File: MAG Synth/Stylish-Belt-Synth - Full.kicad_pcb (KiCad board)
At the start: 2 copper layers, 177.8 x 101.7 mm, 67 parts, among them J0 USB_B, J1 Audio-Jack-3_2Switches, J26 WRITE PATCH, J27 PARAM SELECT, J28 PATCH SELECT, J29 MODE, J30 STYLUS, SW1 Power, U1 stm32f103c8t6-module-china, U2 XPT8871

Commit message: V3 board V2.4 case
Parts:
- removed BT1: 4 x 1.5V, Pin_Headers:Pin_Header_Straight_1x02_Pitch2.54mm
- removed BT2: Conn_01x02, Pin_Headers:Pin_Header_Straight_1x02_Pitch2.54mm
- removed JA1: Conn_01x06, Pin_Headers:Pin_Header_Straight_1x06_Pitch2.54mm
- removed JL1: ~, Pin_Headers:Pin_Header_Straight_1x04_Pitch2.54mm
- removed the REF** at (215.1, 104.8)
- removed the REF** at (82.9, 104.6)
- added ?: 1pin, Connect:1pin, F.Cu at (79.2, 66.4)
- added ?: 1pin, Connect:1pin, F.Cu at (222.1, 70.2)
- added BT12: ~, SoftEggKiCAD:AA_Battery_Dual_Terminal, B.Cu at (95.2, 134.2)
- added BT34: ~, SoftEggKiCAD:AA_Battery_Dual_Terminal, B.Cu at (187.3, 134.0)
- added BTN1: -, SoftEggKiCAD:AA_Battery_-_Terminal, B.Cu at (109.2, 78.1)
- added BTN3: -, SoftEggKiCAD:AA_Battery_-_Terminal, B.Cu at (201.3, 78.1)
- added BTP2: +, SoftEggKiCAD:AA_Battery_+_Terminal, B.Cu at (95.2, 78.1)
- added BTP4: +, SoftEggKiCAD:AA_Battery_+_Terminal, B.Cu at (187.3, 78.1)
- added C2: 1000μF, Capacitors_ThroughHole:CP_Radial_D10.0mm_P5.00mm, B.Cu at (194.2, 66.3)
- added C3: 470μF, Capacitors_ThroughHole:CP_Radial_D10.0mm_P5.00mm, B.Cu at (183.4, 66.3)
- added RA1: 100Ω, SoftEggKiCAD:R_Axial_DIN0204_L3.6mm_D1.6mm_P7.62mm_Horizontal+SMD804, F.Cu at (108.0, 64.1)
- added REF**: 1pin, Connectors:1pin, F.Cu at (215.9, 82.5)
- added REF**: 1pin, Connectors:1pin, F.Cu at (215.9, 91.4)
- added RV1: Volume, SoftEggKiCAD:Wheel_Pot_W_Switch_RV12_B103_FUSTAR, B.Cu at (94.2, 59.4)
- CA1: footprint Capacitors_ThroughHole:CP_Radial_Tantal_D4.5mm_P2.50mm -> SoftEggKiCAD:C_Disc_D5.0mm_W2.5mm_P5.00mm+SMD
- CA3: footprint SoftEggKiCAD:C_Disc_D5.0mm_W2.5mm_P5.00mm+SMD -> Capacitors_ThroughHole:CP_Radial_Tantal_D4.5mm_P2.50mm
- CA4: moved to F.Cu
- J1: value Audio-Jack-3_2Switches -> Headphone
- LS1: value SPEAKER -> Speaker
- R1: value 10kΩ -> 8Ω
- R2: value 1k -> 47Ω
- R3: value 100Ω -> 120Ω; moved to F.Cu
- SW1: value Power -> OVERDRIVE; footprint SoftEggKiCAD:MSS22D18+THT -> Pin_Headers:Pin_Header_Straight_1x03_Pitch2.54mm; moved to B.Cu
- moved G*** 96.7 mm to (196.8, 86.7)
- moved CA4 83.0 mm to (104.8, 58.3), turned to 270 degrees
- moved R2 79.6 mm to (100.6, 66.5)
- moved D3 78.3 mm to (87.6, 72.4), turned to 180 degrees
- moved C1 76.5 mm to (114.9, 67.0), turned to 270 degrees
- moved R1 76.3 mm to (111.8, 66.8), turned to 270 degrees
- moved SW1 70.9 mm to (108.6, 70.5), turned to 90 degrees
- moved R3 67.6 mm to (125.2, 108.1)
- moved CA1 39.9 mm to (174.0, 56.8), turned to 270 degrees
- moved U2 36.5 mm to (189.2, 61.0), turned to 90 degrees
- moved CA2 35.0 mm to (177.8, 56.5), turned to 270 degrees
- moved CA3 34.0 mm to (181.9, 59.7)
- moved D4 31.8 mm to (87.6, 70.0), turned to 0 degrees
- moved D1 16.1 mm to (102.4, 83.1), turned to 180 degrees
- moved CL0 6.46 mm to (148.5, 60.2), turned to 45 degrees
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- renumbered REF** to ?
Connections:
- C1 pad 1: /PWM_OUT -> Net-(C1-Pad1)
- C1 pad 2: Net-(C1-Pad2) -> GND
- CL0 pad 1: /+5V -> /VIN
- CL1 pad 1: /+5V -> /VIN
- CL10 pad 1: /+5V -> /VIN
- CL11 pad 1: /+5V -> /VIN
- CL12 pad 1: /+5V -> /VIN
- CL13 pad 1: /+5V -> /VIN
- CL14 pad 1: /+5V -> /VIN
- CL15 pad 1: /+5V -> /VIN
- CL2 pad 1: /+5V -> /VIN
- CL3 pad 1: /+5V -> /VIN
- CL4 pad 1: /+5V -> /VIN
- CL5 pad 1: /+5V -> /VIN
- CL6 pad 1: /+5V -> /VIN
- CL7 pad 1: /+5V -> /VIN
- CL8 pad 1: /+5V -> /VIN
- CL9 pad 1: /+5V -> /VIN
- D3 pad 1: /+5V -> /VUSB
- D3 pad 2: Net-(D3-Pad2) -> Net-(BTP4-Pad1)
- D4 pad 1: /+5V -> /VUSB
- J1 pad 1: /XH-M125-amp-board/OUT+ -> Net-(J1-Pad1)
- J1 pad 2: /XH-M125-amp-board/OUT+ -> Net-(J1-Pad1)
- J1 pad 3: /XH-M125-amp-board/OUT- -> Net-(J1-Pad3)
- LS1 pad 2: /XH-M125-amp-board/OUT- -> Net-(J1-Pad3)
- R1 pad 1: Net-(C1-Pad2) -> Net-(C1-Pad1)
- R2 pad 1: GND -> Net-(R2-Pad1)
- R2 pad 2: Net-(C1-Pad2) -> Net-(C1-Pad1)
- R3 pad 1: Net-(R3-Pad1) -> /VIN
- R3 pad 2: Net-(CA4-Pad1) -> /+3.3V
- RGB0 pad 1: /+5V -> /VIN
- RGB1 pad 1: /+5V -> /VIN
- RGB10 pad 1: /+5V -> /VIN
- RGB11 pad 1: /+5V -> /VIN
- RGB12 pad 1: /+5V -> /VIN
- RGB13 pad 1: /+5V -> /VIN
- RGB14 pad 1: /+5V -> /VIN
- RGB15 pad 1: /+5V -> /VIN
- RGB15 pad 2: /WS2812B-16-LED-RING/DOUT -> /DOUT
- RGB2 pad 1: /+5V -> /VIN
- RGB3 pad 1: /+5V -> /VIN
- RGB4 pad 1: /+5V -> /VIN
- RGB5 pad 1: /+5V -> /VIN
- RGB6 pad 1: /+5V -> /VIN
- RGB7 pad 1: /+5V -> /VIN
- RGB8 pad 1: /+5V -> /VIN
- RGB9 pad 1: /+5V -> /VIN
- U1 pad 38: Net-(U1-Pad38) -> /+3.3V
- U2 pad 4: Net-(R3-Pad1) -> Net-(RA1-Pad1)
- U2 pad 5: /XH-M125-amp-board/OUT+ -> Net-(J1-Pad3)
- U2 pad 8: /XH-M125-amp-board/OUT- -> Net-(J1-Pad1)
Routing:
- net Net-(BTP4-Pad1): track 0.00 -> 330.3 mm
- net Net-(BTN3-Pad1): track 0.00 -> 317.1 mm
- net /VIN: track 0.00 -> 248.2 mm, vias 0 -> 16
- net GND: track 549.0 -> 728.0 mm, vias 17 -> 18
- net /+3.3V: track 0.00 -> 166.0 mm, vias 0 -> 1
- net /AUDIO_OUT: track 58.4 -> 183.9 mm, vias 0 -> 2
- net /+5V: track 364.2 -> 244.8 mm, vias 21 -> 2
- net /XH-M125-amp-board/OUT+: track 104.1 -> 0.00 mm, vias 3 -> 0
- net Net-(RA1-Pad1): track 0.00 -> 90.2 mm, vias 0 -> 1
- net /XH-M125-amp-board/OUT-: track 84.7 -> 0.00 mm, vias 1 -> 0
- net Net-(J1-Pad1): track 0.00 -> 77.0 mm, vias 0 -> 3
- net /F0: track 111.6 -> 47.4 mm
- net Net-(J1-Pad3): track 0.00 -> 31.1 mm
- net Net-(D4-Pad2): track 6.87 -> 35.3 mm
- net /WRITE: track 151.2 -> 123.9 mm
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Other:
- outline, holes or cut-outs redrawn
- net class Default: trace_width 0.2 -> 0.635; via_dia 2.032 -> 1.524
- board text added: "+5V"
- board text added: "-"
- board text added: "3.3V"
- board text added: "AUD"
- board text added: "L"
- board text removed: "+5"
- board text removed: "."
- board text removed: "MODE"
- board text removed: "OUT+"
- board text removed: "OUT-"
- board text removed: "PATCH"
- board text removed: "VALUE"
- board text removed: "VCC"
- board text removed: "WRITE"

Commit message: Updated PCB and V2 Enclosure back
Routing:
- net Net-(BTP4-Pad1): track 330.3 -> 344.5 mm
- net /PARAM: track 135.5 -> 122.5 mm
- net /C#0: track 70.9 -> 81.7 mm
- net /G0: track 150.3 -> 140.0 mm
- net /E1: track 46.6 -> 56.2 mm
- net /VIN: track 248.2 -> 257.4 mm
- net /F1: track 51.1 -> 42.3 mm
- net Net-(BTN3-Pad1): track 317.1 -> 325.6 mm
- net /G#0: track 164.3 -> 157.5 mm
- net /A1: track 89.6 -> 96.1 mm
- net /+5V: track 244.8 -> 238.8 mm
- net /E0: track 56.3 -> 60.7 mm
- net /+3.3V: track 166.0 -> 161.6 mm
- net /PATCH: track 111.5 -> 108.0 mm
- net Net-(J1-Pad1): track 77.0 -> 73.7 mm
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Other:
- board text added: "5"
- board text added: "G"
- board text removed: "+5V"

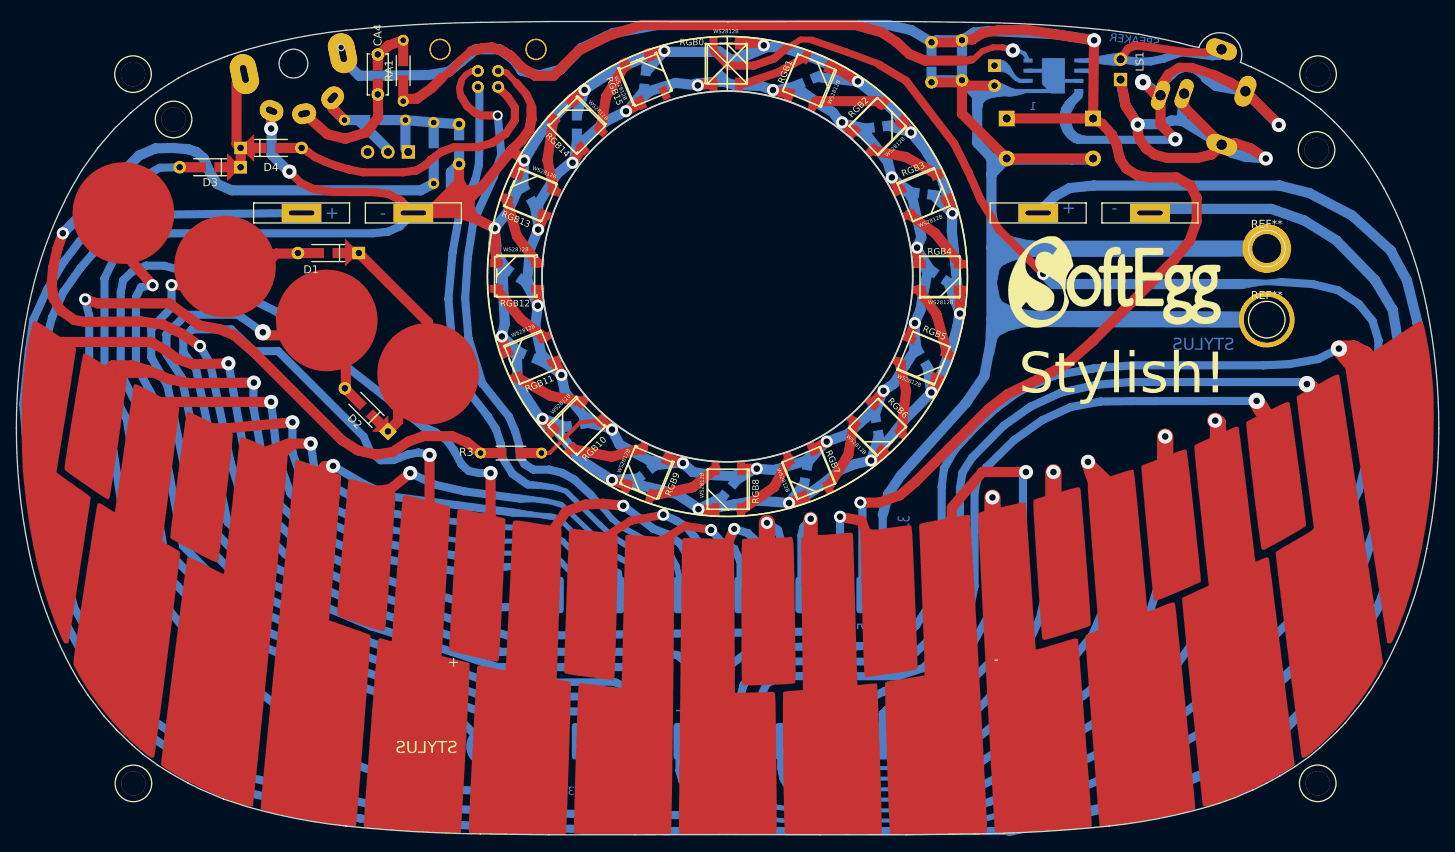
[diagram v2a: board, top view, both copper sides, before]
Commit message: More board cleanup. Fixed values of parts based on test board construction. Rewired potentiometer so that low volume is nearest the power on/off click. More hand vias where they are needed.
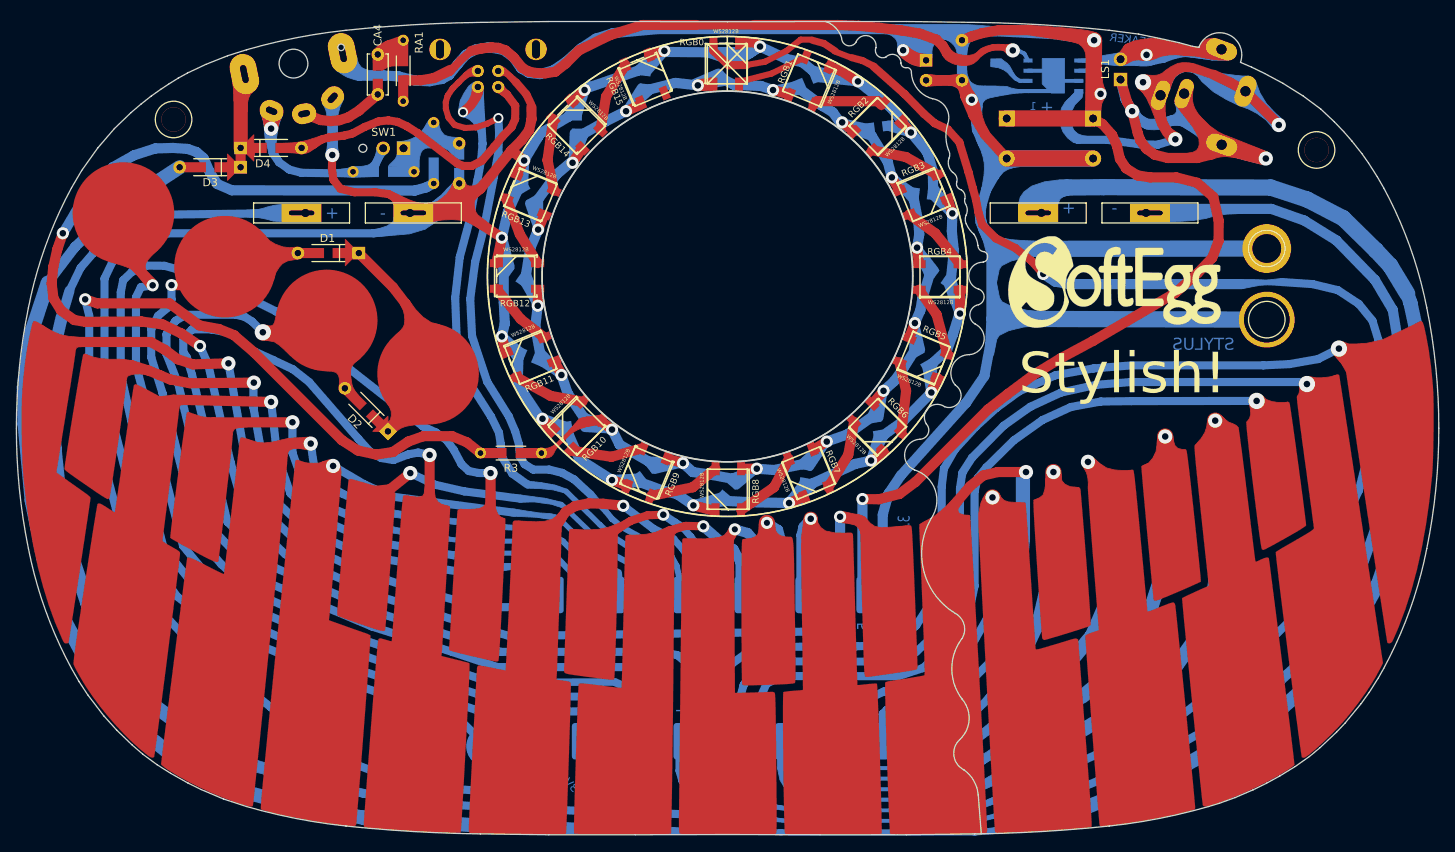
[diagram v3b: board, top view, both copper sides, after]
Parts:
- removed the ? at (74.2, 60.8)
- removed the ? at (222.3, 60.8)
- removed the ? at (222.3, 149.4)
- removed the ? at (74.2, 149.4)
- added BT12H1: Battery, SoftEggKiCAD:BatteryHolder_Keystone_2462_2xAA_MOD, B.Cu at (94.8, 78.1)
- added BT34H1: Battery, SoftEggKiCAD:BatteryHolder_Keystone_2462_2xAA_MOD, B.Cu at (186.8, 78.1)
- ? (x2): value 1pin -> ~
- CA1: footprint SoftEggKiCAD:C_Disc_D5.0mm_W2.5mm_P5.00mm+SMD -> Capacitors_ThroughHole:CP_Radial_Tantal_D4.5mm_P2.50mm
- CA3: footprint Capacitors_ThroughHole:CP_Radial_Tantal_D4.5mm_P2.50mm -> SoftEggKiCAD:C_1509
- R2: value 47Ω -> 47KΩ
- R3: value 120Ω -> 44Ω
- ~ (x2): renamed from REF**; value 1pin -> ~
- moved R2 6.55 mm to (101.7, 73.0)
- moved C1 2.41 mm to (115.0, 69.4)
- moved CA1 2.36 mm to (173.3, 59.0)
- moved CA3 1.19 mm to (182.2, 60.8)
- moved SW1 0.76 mm to (108.0, 70.0)
- renumbered G*** to ~
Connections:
- RV1 pad : /+5V -> (no net)
- RV1 pad 1: Net-(R2-Pad1) -> GND
- RV1 pad 3: GND -> Net-(R2-Pad1)
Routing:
- net Net-(R2-Pad1): track 14.1 -> 26.8 mm, vias 0 -> 1
- net /+5V: track 238.8 -> 251.0 mm, vias 2 -> 4
- net /C#0: track 81.7 -> 74.4 mm
- net Net-(J0-Pad2): track 78.2 -> 85.4 mm, vias 0 -> 1
- net GND: track 726.3 -> 721.8 mm
- net /E0: track 60.7 -> 56.2 mm
- net /PWM_OUT: track 14.8 -> 10.4 mm
- net Net-(J0-Pad3): track 85.3 -> 89.0 mm
- net Net-(BT12H1-Pad1): track 325.6 -> 321.9 mm
- net /G1: track 75.7 -> 72.4 mm
- net /C2: track 116.3 -> 113.6 mm
- net Net-(BT34H1-Pad1): track 344.5 -> 341.8 mm
- net /VIN: track 257.4 -> 259.9 mm
- net Net-(D4-Pad2): track 34.4 -> 36.7 mm
- net /G0: track 140.0 -> 138.7 mm
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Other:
- outline, holes or cut-outs redrawn
- board text removed: "GND"

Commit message: PCB V4 update Wood CNC models added
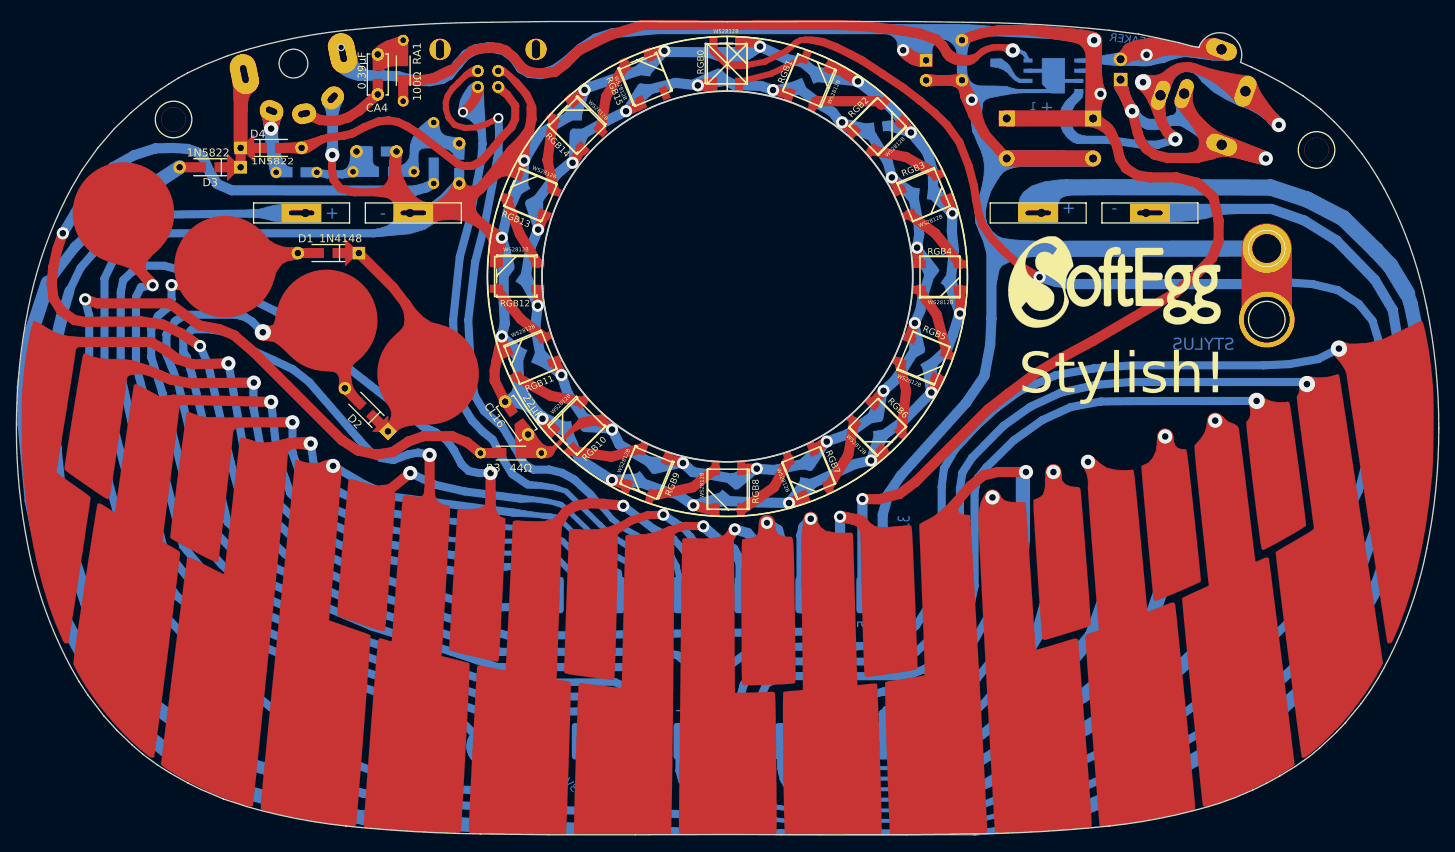
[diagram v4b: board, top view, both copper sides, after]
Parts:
- removed SW1: OVERDRIVE, Pin_Headers:Pin_Header_Straight_1x03_Pitch2.54mm
- added C4: 4.7nF, SoftEggKiCAD:C_Disc_D5.0mm_W2.5mm_P5.00mm+SMD, B.Cu at (102.1, 70.4)
- added CL16: 22µF, SoftEggKiCAD:C_Disc_D5.0mm_W2.5mm_P5.00mm+SMD, F.Cu at (123.6, 105.8)
- added R4: 33kΩ, SoftEggKiCAD:R_Axial_DIN0204_L3.6mm_D1.6mm_P5mm_Horizontal+SMD804, B.Cu at (90.8, 73.0)
- C1: value 1μF -> 220nF
- R1: value 8Ω -> 330Ω
- R2: value 47KΩ -> 3.3kΩ
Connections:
- R2 pad 1: Net-(R2-Pad1) -> Net-(C4-Pad1)
- RV1 pad 3: Net-(R2-Pad1) -> Net-(RR4-Pad1)
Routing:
- net Net-(R2-Pad1): track 26.8 -> 0.00 mm, vias 1 -> 0
- net Net-(RR4-Pad1): track 0.00 -> 14.5 mm, vias 0 -> 1
- net Net-(C4-Pad1): track 0.00 -> 7.16 mm
- net GND: track 721.8 -> 715.8 mm
- net /VIN: track 259.9 -> 262.7 mm
- net Net-(C1-Pad1): track 11.3 -> 9.87 mm
- net Net-(J0-Pad3): track 89.0 -> 89.7 mm
- net Net-(J0-Pad2): track 85.4 -> 86.1 mm
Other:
- outline, holes or cut-outs redrawn

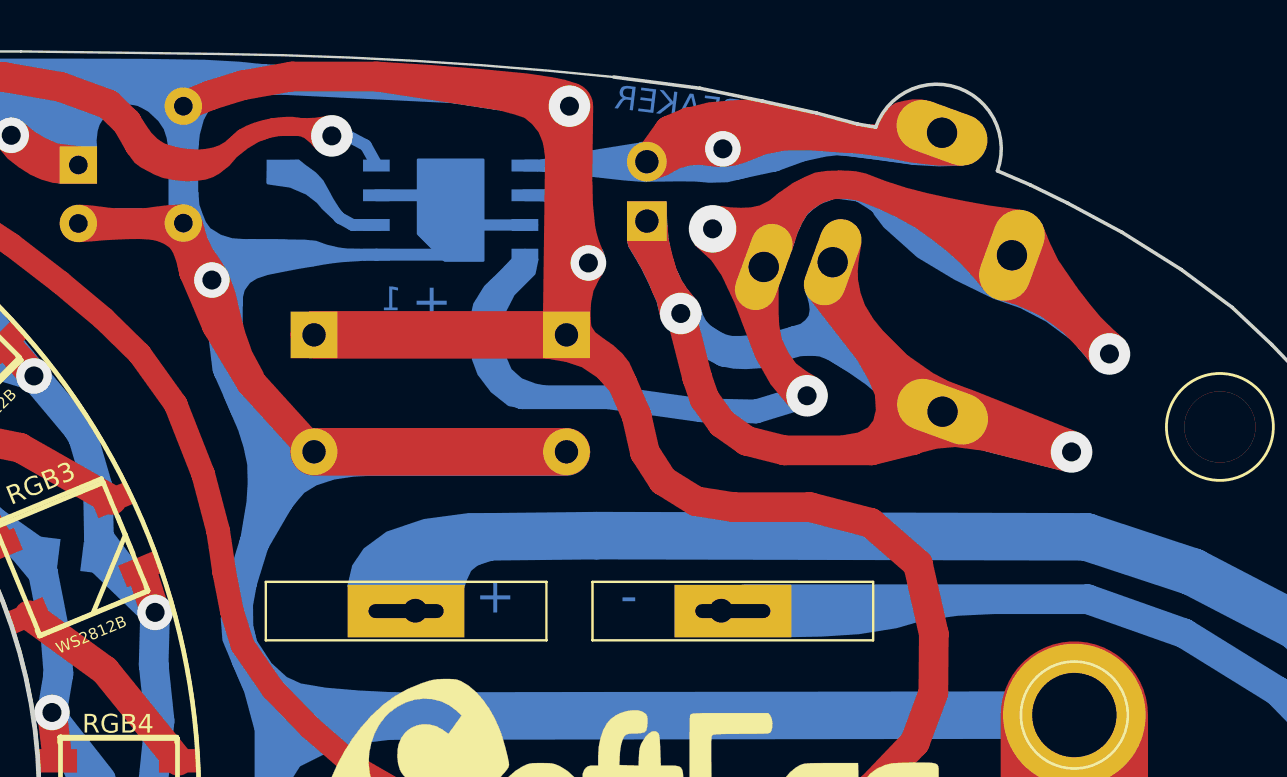
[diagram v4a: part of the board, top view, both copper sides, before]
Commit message: Small updates to PCB. One footprint changed so all SMD are 0805. BOM added. V1 of Source Code added.
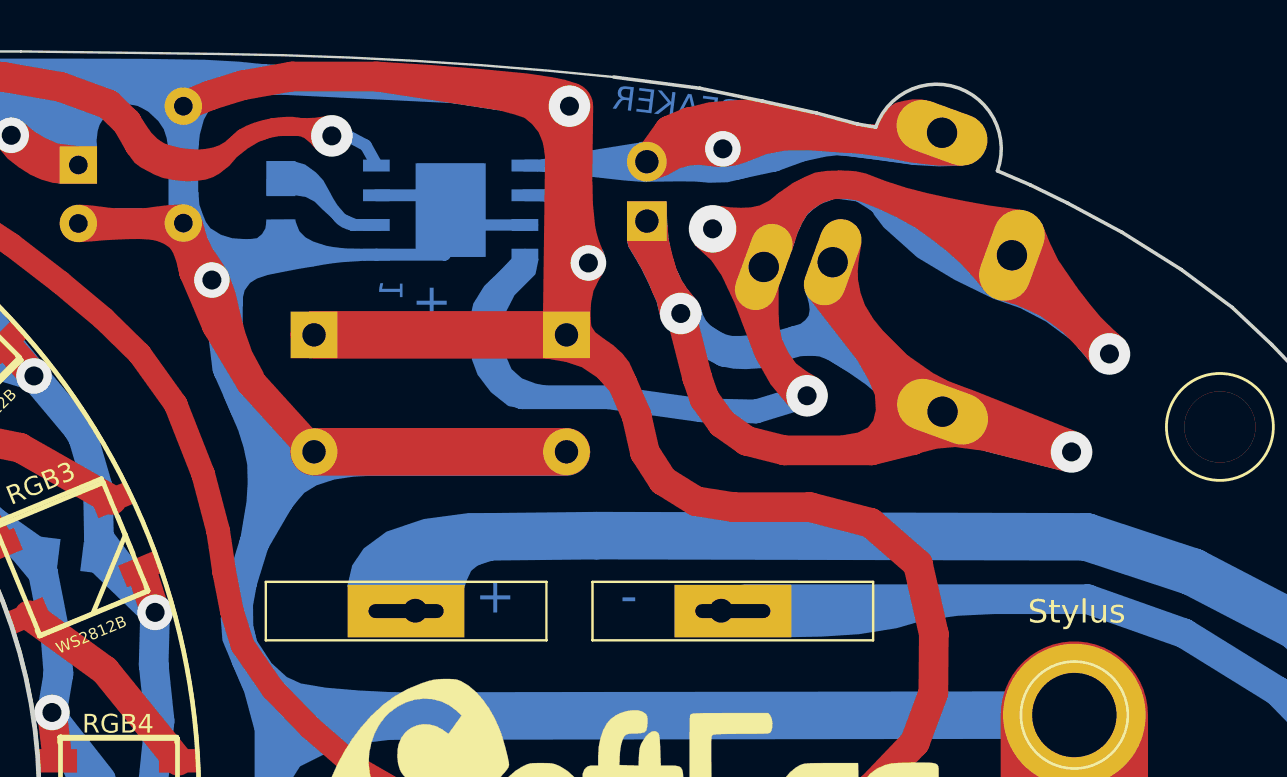
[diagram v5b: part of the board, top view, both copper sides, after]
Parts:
- CA1: value 470μF -> 220μF
- CA3: footprint SoftEggKiCAD:C_1509 -> Capacitors_SMD:C_0805_HandSoldering
- LS1: value Speaker -> SPEAKER
- Stylus: renamed from ~; value ~ -> Stylus
- U2: footprint SMD_Packages:SOIC-8-N -> SoftEggKiCAD:SOIC-8-N-TP
- moved CA3 0.24 mm to (182.0, 60.9)
